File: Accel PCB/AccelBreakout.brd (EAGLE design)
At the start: 17.8 x 14.3 mm, 8 parts

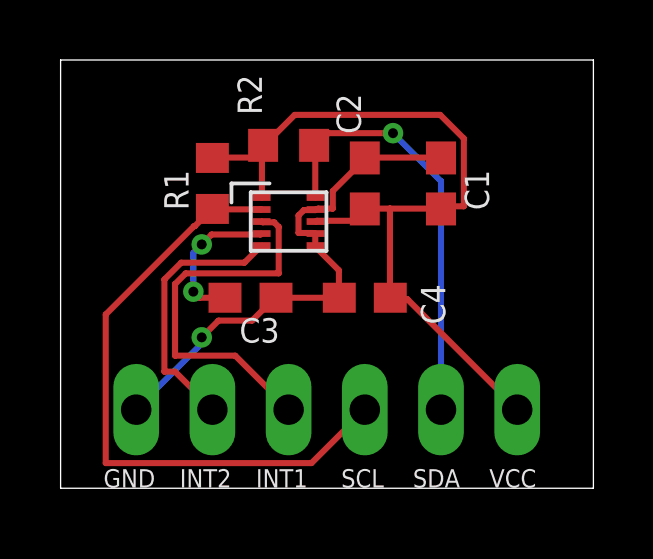
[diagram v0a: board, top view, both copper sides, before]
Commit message: Minimized the Accel PCB layout
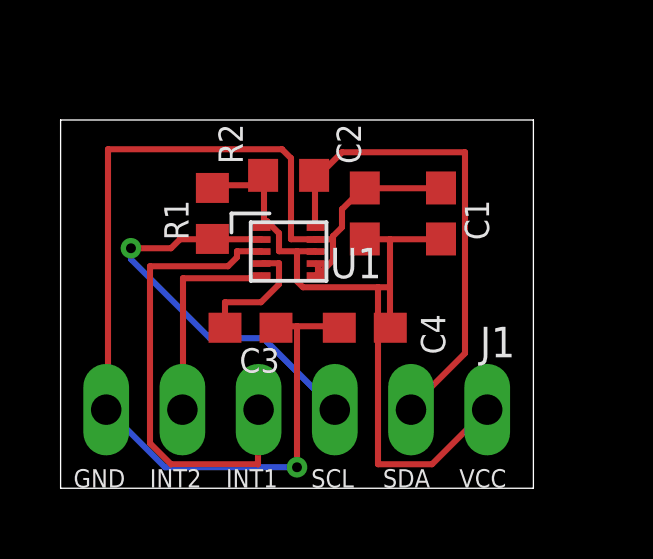
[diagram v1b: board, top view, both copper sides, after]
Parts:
- moved SV1 1.00 mm to (7.89, 2.62)
- moved U$23 1.00 mm to (7.62, 7.89)
- moved C1 1.00 mm to (12.7, 9.16)
- moved C2 1.00 mm to (10.2, 9.16)
- moved C3 1.00 mm to (6.35, 5.35)
- moved C4 1.00 mm to (10.2, 5.35)
- moved R1 1.00 mm to (5.08, 9.16)
- moved R2 1.00 mm to (7.62, 10.4)
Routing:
- net GND: track 18.0 -> 39.8 mm
- net SCL: track 21.0 -> 13.7 mm, vias 0 -> 1
- net INT1: track 12.7 -> 15.7 mm
- net SDA: track 14.5 -> 16.5 mm, vias 1 -> 0
- net INT2: track 8.92 -> 7.07 mm
- net VCC: track 27.4 -> 26.3 mm
- net N$34: track 4.97 -> 4.18 mm, vias 2 -> 0
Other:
- board size 17.8 x 14.3 mm -> 15.8 x 12.3 mm
- board text added: "J1"
- board text added: "U1"

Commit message: Fixed silk screen and added accelerometer directions
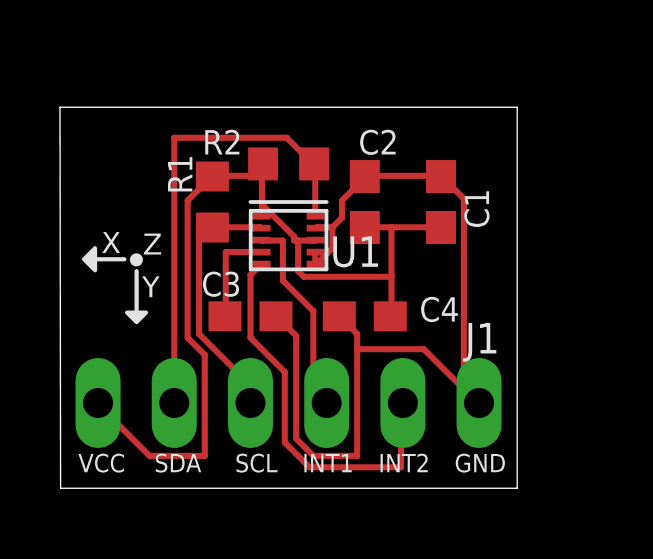
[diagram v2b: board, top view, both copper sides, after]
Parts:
- removed SV1: (no value), con-lstb:MA06-1
- added U$1: DIP1X6MALE, ScottSilver:DIP1X6MALE
- added U$2: ACCELDIR, ScottSilver:ACCELDIR
- moved U$23 0.38 mm to (7.62, 8.27)
- moved C1 0.38 mm to (12.7, 9.54)
- moved C2 0.38 mm to (10.2, 9.54)
- moved C3 0.38 mm to (6.35, 5.73)
- moved C4 0.38 mm to (10.2, 5.73)
- moved R1 0.38 mm to (5.08, 9.54)
- moved R2 0.38 mm to (7.62, 10.8)
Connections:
- net GND: now also U$1.6; no longer SV1.6
- net INT1: now also U$1.4; no longer SV1.4
- net INT2: now also U$1.5; no longer SV1.5
- net SCL: now also U$1.3; no longer SV1.3
- net SDA: now also U$1.2; no longer SV1.2
- net VCC: now also U$1.1; no longer SV1.1
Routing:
- net INT1: track 15.7 -> 6.76 mm
- net GND: track 39.8 -> 31.6 mm, vias 1 -> 0
- net INT2: track 7.07 -> 13.0 mm
- net SCL: track 13.7 -> 8.42 mm, vias 1 -> 0
- net VCC: track 26.3 -> 30.2 mm
- net N$34: track 4.18 -> 3.34 mm
- net SDA: track 16.5 -> 15.7 mm
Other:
- board size 15.8 x 12.3 mm -> 15.2 x 12.7 mm

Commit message: Fixed text and arrow orientaiton for accel PCB
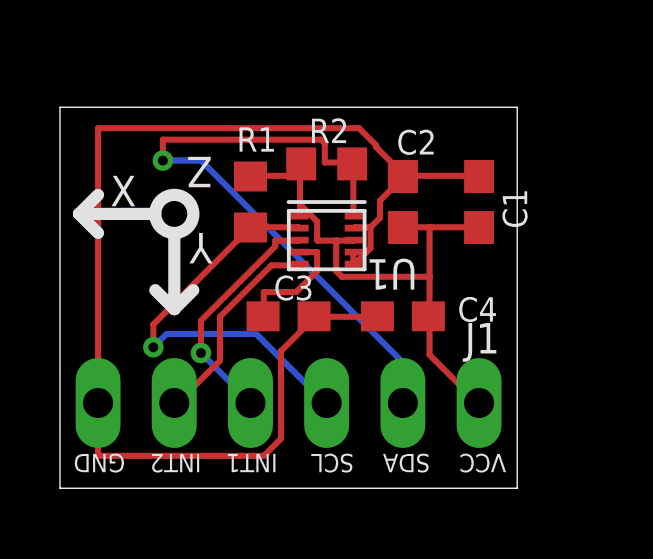
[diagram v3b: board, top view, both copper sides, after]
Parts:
- moved U$2 1.55 mm to (3.81, 8.51)
- moved C1 1.27 mm to (14.0, 9.54)
- moved C3 1.27 mm to (7.62, 5.73)
- moved R2 1.27 mm to (8.89, 10.8)
- moved U$23 1.27 mm to (8.89, 8.27)
- moved C2 1.27 mm to (11.4, 9.54)
- moved C4 1.27 mm to (11.4, 5.73)
- moved R1 1.27 mm to (6.35, 9.54)
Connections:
- net GND: now also U$1.1; no longer U$1.6
- net INT1: now also U$1.3; no longer U$1.4
- net INT2: now also U$1.2; no longer U$1.5
- net SCL: now also U$1.4; no longer U$1.3
- net SDA: now also U$1.5; no longer U$1.2
- net VCC: now also U$1.6; no longer U$1.1
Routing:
- net GND: track 31.6 -> 42.0 mm
- net VCC: track 30.2 -> 19.9 mm
- net SDA: track 15.7 -> 23.1 mm, vias 0 -> 1
- net INT2: track 13.0 -> 6.96 mm
- net SCL: track 8.42 -> 13.9 mm, vias 0 -> 1
- net INT1: track 6.76 -> 7.94 mm, vias 0 -> 1
- net N$34: track 3.34 -> 4.10 mm

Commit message: Split 1x6 header into 2 1x3 headers 300 mils apart to fit over center bridge on breadboard
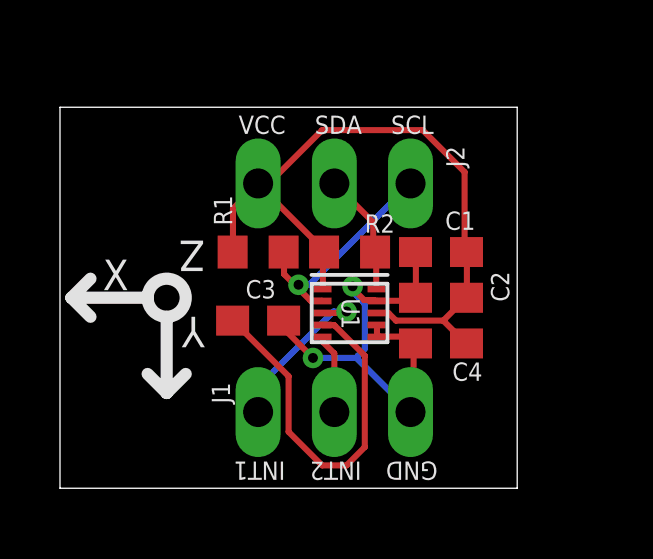
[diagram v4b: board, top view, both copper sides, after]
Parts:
- removed U$1: DIP1X6MALE, ScottSilver:DIP1X6MALE
- added U$3, U$4: DIP1X3MALE, OldScottSilver:DIP1X3MALE
- moved C2 3.43 mm to (12.7, 6.35), turned to 180 degrees
- moved R2 3.03 mm to (9.65, 7.87)
- moved U$2 2.81 mm to (3.56, 5.71)
- moved U$23 2.55 mm to (9.65, 5.84)
- moved C1 2.10 mm to (12.7, 7.87), turned to 180 degrees
- moved R1 1.69 mm to (6.60, 7.87), turned to 180 degrees
- moved C4 1.56 mm to (12.7, 4.83)
- moved C3 1.03 mm to (6.60, 5.59)
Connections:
- net GND: now also U$4.P$3; no longer U$1.1
- net INT1: now also U$4.P$1; no longer U$1.3
- net INT2: now also U$4.P$2; no longer U$1.2
- net SCL: now also U$3.P$3; no longer U$1.4
- net SDA: now also U$3.P$2; no longer U$1.5
- net VCC: now also U$3.P$1; no longer U$1.6
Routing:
- net GND: track 42.0 -> 16.4 mm, vias 0 -> 2
- net SDA: track 23.1 -> 4.11 mm, vias 1 -> 0
- net N$34: track 4.10 -> 12.6 mm
- net SCL: track 13.9 -> 7.63 mm
- net INT2: track 6.96 -> 2.66 mm
- net VCC: track 19.9 -> 24.1 mm
- net INT1: track 7.94 -> 5.65 mm
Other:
- board text added: "J2"
